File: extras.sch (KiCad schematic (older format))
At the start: 36 parts, among them P1 CONN_01X03, P2 CONN_01X03, P3 CONN_01X02, P4 CONN_01X02, P5 CONN_01X02, P6 CONN_01X02, U1 LT3472, U2 LMR62014, U3 LM3674

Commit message: Latest work
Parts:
- added C?: 2.2uF, symbol C
- added C?: 47pF, symbol C_Small
- added C?: 22uF, symbol C
- added C? (x2): 0.1uF, symbol C_Small
- added C?: 4.7uF, symbol C
- added L? (x2): 15uH, symbol L_Small
- added L?: 10uH, symbol L_Small
- added R?: 324k, symbol R_Small
- added R?: 549k, symbol R_Small
- added U?: LT3487, symbol LT3487
- R5: value 117k -> 118k
- U1: symbol LT3472-RESCUE-PowerRail -> LT3472
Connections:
- net labels added: -8.1V/90mA, 14.95V/45mA, CAP, FBN, FBP, RUN/SS, VIN_3V_12V
- wire segments 82 -> 161
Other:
- note added: "VNEG = -RN * 0.025 [mA] \n(40 kOhm : 1 V)"
- note added: "VPOS = 1.23 + RN * 0.025 [mA] \n(40 kOhm : 1 V)"
- moved on the sheet: P3, P4, P5, P6

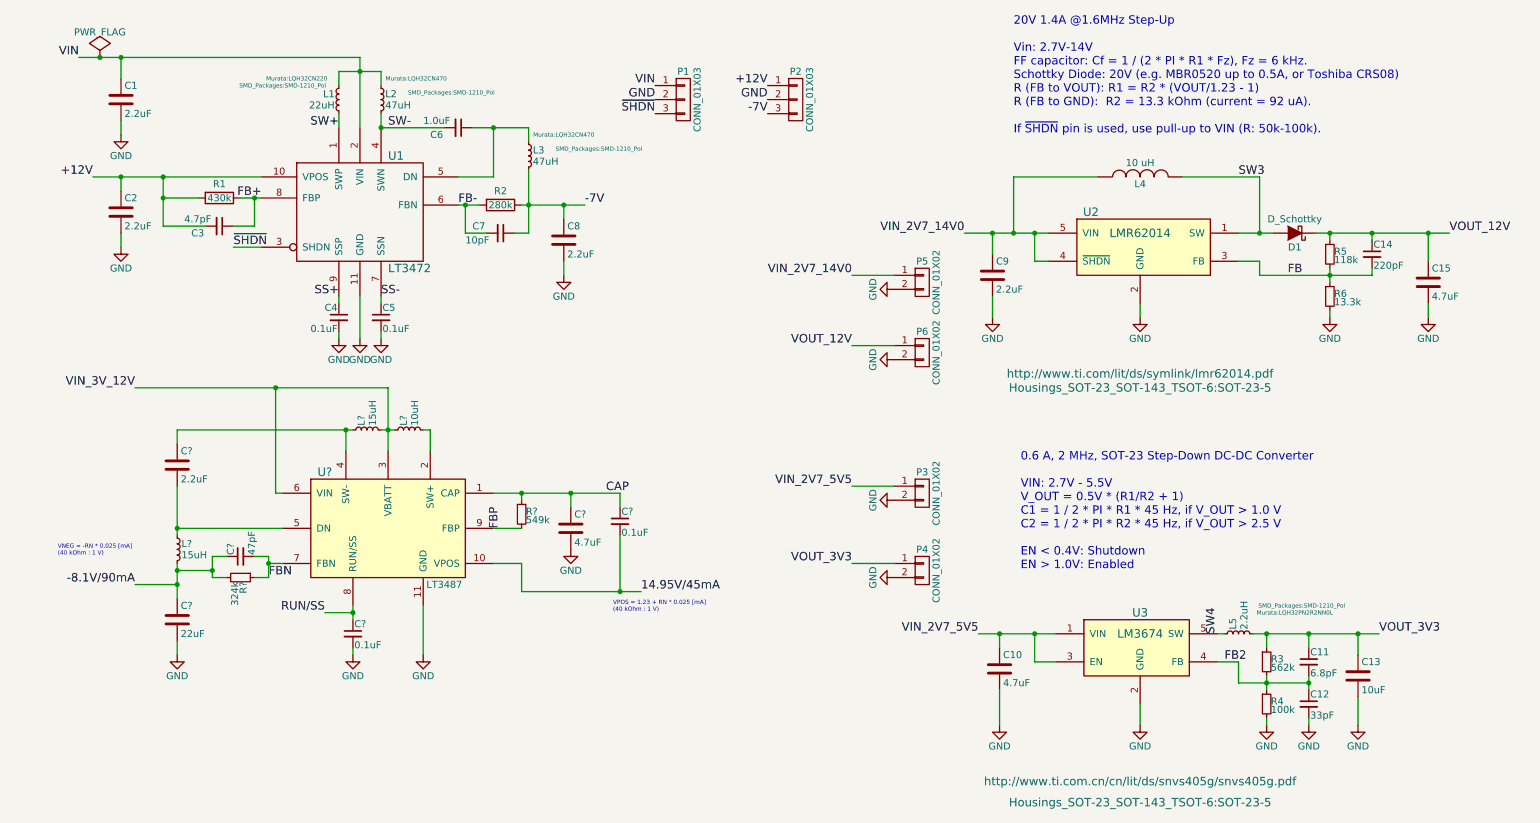
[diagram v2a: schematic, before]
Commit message: Follow ADISimPower recommendations
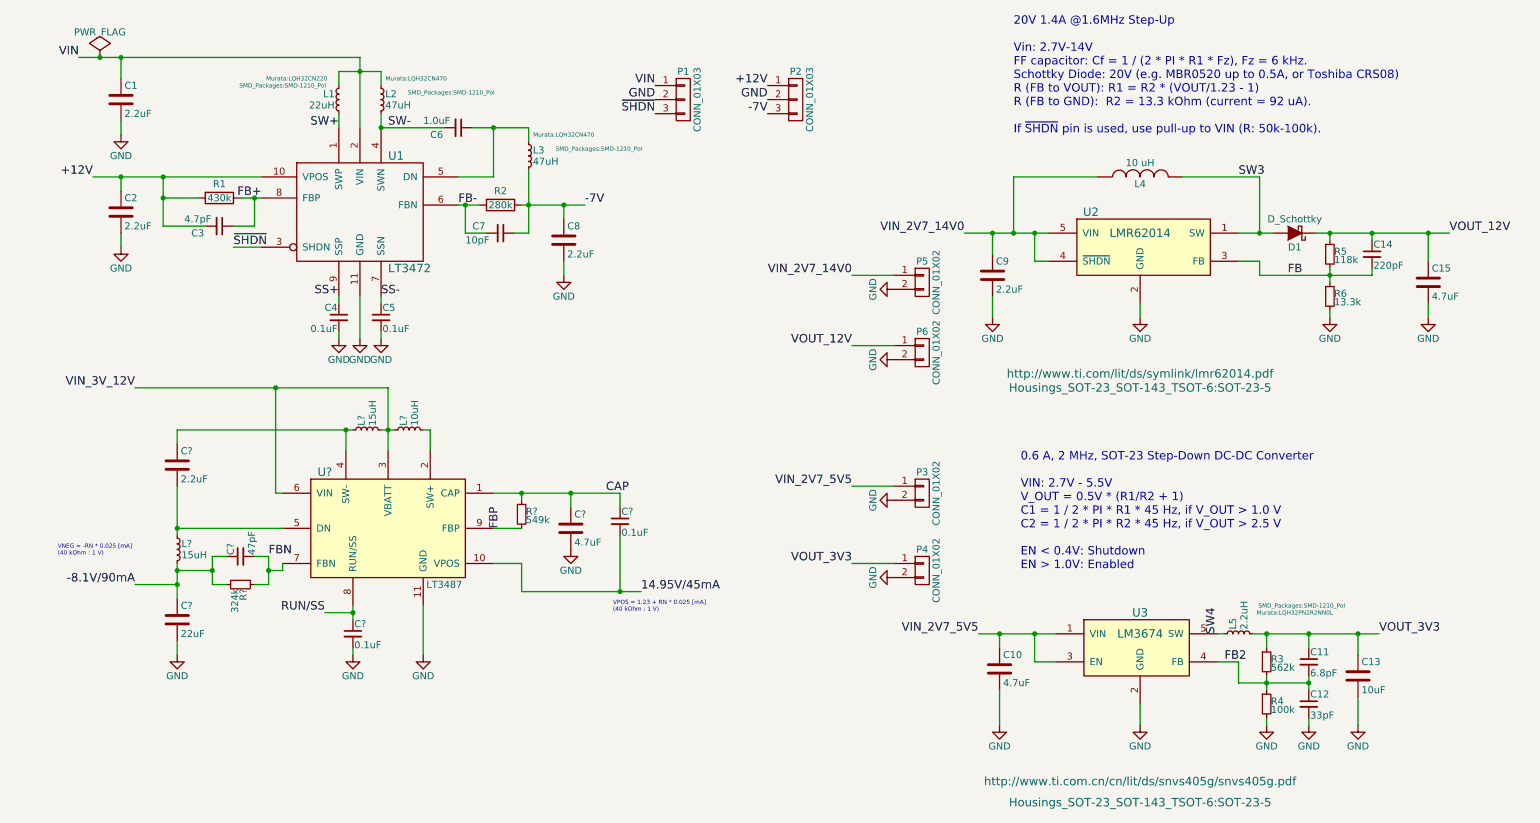
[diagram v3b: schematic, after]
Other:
- moved on the sheet: R?
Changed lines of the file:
@@
 $EndDescr
 Wire Wire Line
-	1050 950  1200 950
-Wire Wire Line
-	1200 950  1350 950
-Wire Wire Line
-	1350 950  3050 950
+	1050 950  3050 950
 $Comp
 L C C1
@@
 	2900 1150 2900 1050
 Wire Wire Line
-	2900 1050 3050 1050
-Wire Wire Line
-	3050 1050 3200 1050
+	2900 1050 3200 1050
 Connection ~ 3050 1050
 Wire Wire Line
@@
 $EndComp
 Wire Wire Line
-	1150 1800 1350 1800
-Wire Wire Line
-	1350 1800 1650 1800
-Wire Wire Line
-	1650 1800 2350 1800
-Wire Wire Line
-	2200 1950 2300 1950
-Wire Wire Line
-	2300 1950 2350 1950
+	1150 1800 2350 1800
+Wire Wire Line
+	2200 1950 2350 1950
 Wire Wire Line
 	1900 1950 1650 1950
 Wire Wire Line
-	1650 1800 1650 1950
-Wire Wire Line
-	1650 1950 1650 2150
+	1650 1800 1650 2150
 Connection ~ 1650 1800
 Wire Wire Line
@@
 $EndComp
 Wire Wire Line
-	3850 1450 4000 1450
-Wire Wire Line
-	4000 1450 4250 1450
-Wire Wire Line
-	4200 2000 4250 2000
-Wire Wire Line
-	4250 2000 4500 2000
-Wire Wire Line
-	4500 2000 4650 2000
-Wire Wire Line
-	4250 1750 4250 2000
-Wire Wire Line
-	4250 2000 4250 2200
-Wire Wire Line
-	3750 2000 3800 2000
-Wire Wire Line
-	3800 2000 3900 2000
+	3850 1450 4250 1450
+Wire Wire Line
+	4200 2000 4650 2000
+Wire Wire Line
+	4250 1750 4250 2200
+Wire Wire Line
+	3750 2000 3900 2000
 $Comp
 L C_Small C7
@@
 VIN_2V7_5V5
 Wire Wire Line
-	7450 5050 7600 5050
-Wire Wire Line
-	7600 5050 7850 5050
-Wire Wire Line
-	7850 5050 8000 5050
+	7450 5050 8000 5050
 $Comp
 L C C10
@@
 	9150 5050 9200 5050
 Wire Wire Line
-	9400 5050 9500 5050
-Wire Wire Line
-	9500 5050 9800 5050
-Wire Wire Line
-	9800 5050 10150 5050
-Wire Wire Line
-	10150 5050 10300 5050
+	9400 5050 10300 5050
 $Comp
 L R_Small R3
@@
 Connection ~ 9500 5050
 Wire Wire Line
-	9500 5350 9500 5400
-Wire Wire Line
-	9500 5400 9500 5450
-Wire Wire Line
-	9300 5400 9500 5400
-Wire Wire Line
-	9500 5400 9800 5400
-Wire Wire Line
-	9800 5350 9800 5400
-Wire Wire Line
-	9800 5400 9800 5450
+	9500 5350 9500 5450
+Wire Wire Line
+	9300 5400 9800 5400
+Wire Wire Line
+	9800 5350 9800 5450
 Connection ~ 9500 5400
 Connection ~ 9800 5400
@@
 20V 1.4A @1.6MHz Step-Up\n\nVin: 2.7V-14V\nFF capacitor: Cf = 1 / (2 * PI * R1 * Fz), Fz = 6 kHz.\nSchottky Diode: 20V (e.g. MBR0520 up to 0.5A, or Toshiba CRS08)\nR (FB to VOUT): R1 = R2 * (VOUT/1.23 - 1)\nR (FB to GND):  R2 = 13.3 kOhm (current = 92 uA).\n\nIf ~SHDN~ pin is used, use pull-up to VIN (R: 50k-100k).
 Wire Wire Line
-	7350 2200 7550 2200
-Wire Wire Line
-	7550 2200 7700 2200
-Wire Wire Line
-	7700 2200 7850 2200
-Wire Wire Line
-	7850 2200 7950 2200
+	7350 2200 7950 2200
 Connection ~ 7850 2200
 Wire Wire Line
@@
 	9450 1800 9450 2200
 Wire Wire Line
-	9300 2200 9450 2200
-Wire Wire Line
-	9450 2200 9550 2200
+	9300 2200 9550 2200
 $Comp
 L D_Schottky D1
@@
 Connection ~ 9450 2200
 Wire Wire Line
-	9850 2200 9950 2200
-Wire Wire Line
-	9950 2200 10250 2200
-Wire Wire Line
-	10250 2200 10650 2200
-Wire Wire Line
-	10650 2200 10800 2200
+	9850 2200 10800 2200
 $Comp
 L R_Small R5
@@
 Connection ~ 10250 2200
 Wire Wire Line
-	9950 2450 9950 2500
-Wire Wire Line
-	9950 2500 9950 2550
-Wire Wire Line
-	9450 2500 9950 2500
-Wire Wire Line
-	9950 2500 10250 2500
+	9950 2450 9950 2550
+Wire Wire Line
+	9450 2500 10250 2500
 Wire Wire Line
 	10250 2500 10250 2450
@@
 SW3
 Wire Wire Line
-	3050 950  3050 1050
-Wire Wire Line
-	3050 1050 3050 1450
+	3050 950  3050 1450
 $Comp
 L LT3487 U?
@@
 	2950 3750 2950 3600
 Wire Wire Line
-	1750 3600 2950 3600
-Wire Wire Line
-	2950 3600 3000 3600
-Wire Wire Line
-	3200 3600 3250 3600
-Wire Wire Line
-	3250 3600 3300 3600
-Wire Wire Line
-	3250 3300 3250 3600
-Wire Wire Line
-	3250 3600 3250 3750
+	1750 3600 3000 3600
+Wire Wire Line
+	3200 3600 3300 3600
+Wire Wire Line
+	3250 3300 3250 3750
 Connection ~ 3250 3600
 Wire Wire Line
-	1450 3300 2450 3300
-Wire Wire Line
-	2450 3300 3250 3300
+	1450 3300 3250 3300
 Wire Wire Line
 	3500 3600 3550 3600
@@
 $EndComp
 Wire Wire Line
-	1750 4000 1750 4300
-Wire Wire Line
-	1750 4300 1750 4350
+	1750 4000 1750 4350
 $Comp
 L C_Small C?
@@
 L R_Small R?
 U 1 1 56573C0F
-P 2200 4650
-F 0 "R?" H 2230 4670 50  0000 L CNN
-F 1 "324k" H 2230 4610 50  0000 L CNN
-F 2 "" H 2200 4650 60  0000 C CNN
-F 3 "" H 2200 4650 60  0000 C CNN
-	1    2200 4650
+P 2200 4700
+F 0 "R?" H 2230 4720 50  0000 L CNN
+F 1 "324k" H 2230 4660 50  0000 L CNN
+F 2 "" H 2200 4700 60  0000 C CNN
+F 3 "" H 2200 4700 60  0000 C CNN
+	1    2200 4700
 	0    1    1    0
 $EndComp
@@
 	2300 4500 2400 4500
 Wire Wire Line
-	2400 4500 2400 4550
-Wire Wire Line
-	2400 4550 2400 4650
-Wire Wire Line
-	2400 4550 2500 4550
-Wire Wire Line
-	2400 4650 2300 4650
-Connection ~ 2400 4550
+	2400 4500 2400 4700
+Wire Wire Line
+	2400 4600 2500 4600
+Wire Wire Line
+	2400 4700 2300 4700
+Connection ~ 2400 4600
 Wire Wire Line
 	2100 4500 2000 4500
 Wire Wire Line
-	2000 4500 2000 4600
-Wire Wire Line
-	2000 4600 2000 4650
-Wire Wire Line
-	2000 4650 2100 4650
+	2000 4500 2000 4700
+Wire Wire Line
+	2000 4700 2100 4700
 Wire Wire Line
 	2000 4600 1750 4600
 Wire Wire Line
-	1750 4550 1750 4600
-Wire Wire Line
-	1750 4600 1750 4700
-Wire Wire Line
-	1750 4700 1750 4800
+	1750 4550 1750 4800
 Connection ~ 2000 4600
 Wire Wire Line
@@
 $EndComp
 Wire Wire Line
-	3000 4850 3000 4900
-Wire Wire Line
-	3000 4900 3000 4950
+	3000 4850 3000 4950
 $Comp
 L GND #PWR?
@@
 	4000 4300 4200 4300
 Wire Wire Line
-	4000 4050 4200 4050
-Wire Wire Line
-	4200 4050 4550 4050
-Wire Wire Line
-	4550 4050 4900 4050
+	4000 4050 4900 4050
 Wire Wire Line
 	4200 4050 4200 4100
@@
 	4200 4550 4200 4750
 Wire Wire Line
-	4200 4750 4900 4750
-Wire Wire Line
-	4900 4750 5050 4750
+	4200 4750 5050 4750
 Wire Wire Line
 	4900 4750 4900 4350
@@
 Text Label 1450 3300 2    60   ~ 0
 VIN_3V_12V
-Text Label 2400 4650 0    60   ~ 0
+Text Label 2400 4500 0    60   ~ 0
 FBN
 Text Label 4050 4300 1    60   ~ 0
@@
 Text Notes 4850 4900 0    30   ~ 0
 VPOS = 1.23 + RN * 0.025 [mA] \n(40 kOhm : 1 V)
+Wire Wire Line
+	2500 4600 2500 4550
 $EndSCHEMATC

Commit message: Some change
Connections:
- net -8.1V/90mA: no longer R?.2
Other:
- moved on the sheet: R?
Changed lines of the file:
@@
 	2900 1150 2900 1050
 Wire Wire Line
-	2900 1050 3200 1050
+	2900 1050 3050 1050
+Wire Wire Line
+	3050 1050 3200 1050
 Connection ~ 3050 1050
 Wire Wire Line
@@
 $EndComp
 Wire Wire Line
-	1150 1800 2350 1800
-Wire Wire Line
-	2200 1950 2350 1950
+	1150 1800 1350 1800
+Wire Wire Line
+	1350 1800 1650 1800
+Wire Wire Line
+	1650 1800 2350 1800
+Wire Wire Line
+	2200 1950 2300 1950
+Wire Wire Line
+	2300 1950 2350 1950
 Wire Wire Line
 	1900 1950 1650 1950
 Wire Wire Line
-	1650 1800 1650 2150
+	1650 1800 1650 1950
+Wire Wire Line
+	1650 1950 1650 2150
 Connection ~ 1650 1800
 Wire Wire Line
@@
 $EndComp
 Wire Wire Line
-	3850 1450 4250 1450
-Wire Wire Line
-	4200 2000 4650 2000
-Wire Wire Line
-	4250 1750 4250 2200
-Wire Wire Line
-	3750 2000 3900 2000
+	3850 1450 4000 1450
+Wire Wire Line
+	4000 1450 4250 1450
+Wire Wire Line
+	4200 2000 4250 2000
+Wire Wire Line
+	4250 2000 4500 2000
+Wire Wire Line
+	4500 2000 4650 2000
+Wire Wire Line
+	4250 1750 4250 2000
+Wire Wire Line
+	4250 2000 4250 2200
+Wire Wire Line
+	3750 2000 3800 2000
+Wire Wire Line
+	3800 2000 3900 2000
 $Comp
 L C_Small C7
@@
 VIN_2V7_5V5
 Wire Wire Line
-	7450 5050 8000 5050
+	7450 5050 7600 5050
+Wire Wire Line
+	7600 5050 7850 5050
+Wire Wire Line
+	7850 5050 8000 5050
 $Comp
 L C C10
@@
 	9150 5050 9200 5050
 Wire Wire Line
-	9400 5050 10300 5050
+	9400 5050 9500 5050
+Wire Wire Line
+	9500 5050 9800 5050
+Wire Wire Line
+	9800 5050 10150 5050
+Wire Wire Line
+	10150 5050 10300 5050
 $Comp
 L R_Small R3
@@
 Connection ~ 9500 5050
 Wire Wire Line
-	9500 5350 9500 5450
-Wire Wire Line
-	9300 5400 9800 5400
-Wire Wire Line
-	9800 5350 9800 5450
+	9500 5350 9500 5400
+Wire Wire Line
+	9500 5400 9500 5450
+Wire Wire Line
+	9300 5400 9500 5400
+Wire Wire Line
+	9500 5400 9800 5400
+Wire Wire Line
+	9800 5350 9800 5400
+Wire Wire Line
+	9800 5400 9800 5450
 Connection ~ 9500 5400
 Connection ~ 9800 5400
@@
 20V 1.4A @1.6MHz Step-Up\n\nVin: 2.7V-14V\nFF capacitor: Cf = 1 / (2 * PI * R1 * Fz), Fz = 6 kHz.\nSchottky Diode: 20V (e.g. MBR0520 up to 0.5A, or Toshiba CRS08)\nR (FB to VOUT): R1 = R2 * (VOUT/1.23 - 1)\nR (FB to GND):  R2 = 13.3 kOhm (current = 92 uA).\n\nIf ~SHDN~ pin is used, use pull-up to VIN (R: 50k-100k).
 Wire Wire Line
-	7350 2200 7950 2200
+	7350 2200 7550 2200
+Wire Wire Line
+	7550 2200 7700 2200
+Wire Wire Line
+	7700 2200 7850 2200
+Wire Wire Line
+	7850 2200 7950 2200
 Connection ~ 7850 2200
 Wire Wire Line
@@
 	9450 1800 9450 2200
 Wire Wire Line
-	9300 2200 9550 2200
+	9300 2200 9450 2200
+Wire Wire Line
+	9450 2200 9550 2200
 $Comp
 L D_Schottky D1
@@
 Connection ~ 9450 2200
 Wire Wire Line
-	9850 2200 10800 2200
+	9850 2200 9950 2200
+Wire Wire Line
+	9950 2200 10250 2200
+Wire Wire Line
+	10250 2200 10650 2200
+Wire Wire Line
+	10650 2200 10800 2200
 $Comp
 L R_Small R5
@@
 Connection ~ 10250 2200
 Wire Wire Line
-	9950 2450 9950 2550
-Wire Wire Line
-	9450 2500 10250 2500
+	9950 2450 9950 2500
+Wire Wire Line
+	9950 2500 9950 2550
+Wire Wire Line
+	9450 2500 9950 2500
+Wire Wire Line
+	9950 2500 10250 2500
 Wire Wire Line
 	10250 2500 10250 2450
@@
 SW3
 Wire Wire Line
-	3050 950  3050 1450
+	3050 950  3050 1050
+Wire Wire Line
+	3050 1050 3050 1450
 $Comp
 L LT3487 U?
@@
 	2950 3750 2950 3600
 Wire Wire Line
-	1750 3600 3000 3600
-Wire Wire Line
-	3200 3600 3300 3600
-Wire Wire Line
-	3250 3300 3250 3750
+	1750 3600 2950 3600
+Wire Wire Line
+	2950 3600 3000 3600
+Wire Wire Line
+	3200 3600 3250 3600
+Wire Wire Line
+	3250 3600 3300 3600
+Wire Wire Line
+	3250 3300 3250 3600
+Wire Wire Line
+	3250 3600 3250 3750
 Connection ~ 3250 3600
 Wire Wire Line
-	1450 3300 3250 3300
+	1450 3300 2450 3300
+Wire Wire Line
+	2450 3300 3250 3300
 Wire Wire Line
 	3500 3600 3550 3600
@@
 $EndComp
 Wire Wire Line
-	1750 4000 1750 4350
+	1750 4000 1750 4300
+Wire Wire Line
+	1750 4300 1750 4350
 $Comp
 L C_Small C?
@@
 L R_Small R?
 U 1 1 56573C0F
-P 2200 4700
-F 0 "R?" H 2230 4720 50  0000 L CNN
-F 1 "324k" H 2230 4660 50  0000 L CNN
-F 2 "" H 2200 4700 60  0000 C CNN
-F 3 "" H 2200 4700 60  0000 C CNN
-	1    2200 4700
+P 2200 4650
+F 0 "R?" H 2230 4670 50  0000 L CNN
+F 1 "324k" H 2230 4610 50  0000 L CNN
+F 2 "" H 2200 4650 60  0000 C CNN
+F 3 "" H 2200 4650 60  0000 C CNN
+	1    2200 4650
 	0    1    1    0
 $EndComp
@@
 	2400 4600 2500 4600
 Wire Wire Line
-	2400 4700 2300 4700
-Connection ~ 2400 4600
+	2400 4550 2500 4550
+Wire Wire Line
+	2400 4650 2300 4650
+Connection ~ 2400 4550
 Wire Wire Line
 	2100 4500 2000 4500
@@
 	2000 4600 1750 4600
 Wire Wire Line
-	1750 4550 1750 4800
+	1750 4550 1750 4600
+Wire Wire Line
+	1750 4600 1750 4700
+Wire Wire Line
+	1750 4700 1750 4800
 Connection ~ 2000 4600
 Wire Wire Line
@@
 $EndComp
 Wire Wire Line
-	3000 4850 3000 4950
+	3000 4850 3000 4900
+Wire Wire Line
+	3000 4900 3000 4950
 $Comp
 L GND #PWR?
@@
 	4000 4300 4200 4300
 Wire Wire Line
-	4000 4050 4900 4050
+	4000 4050 4200 4050
+Wire Wire Line
+	4200 4050 4550 4050
+Wire Wire Line
+	4550 4050 4900 4050
 Wire Wire Line
 	4200 4050 4200 4100
@@
 	4200 4550 4200 4750
 Wire Wire Line
-	4200 4750 5050 4750
+	4200 4750 4900 4750
+Wire Wire Line
+	4900 4750 5050 4750
 Wire Wire Line
 	4900 4750 4900 4350
@@
 Text Label 1450 3300 2    60   ~ 0
 VIN_3V_12V
-Text Label 2400 4500 0    60   ~ 0
+Text Label 2400 4650 0    60   ~ 0
 FBN
 Text Label 4050 4300 1    60   ~ 0
@@
 Text Notes 4850 4900 0    30   ~ 0
 VPOS = 1.23 + RN * 0.025 [mA] \n(40 kOhm : 1 V)
-Wire Wire Line
-	2500 4600 2500 4550
 $EndSCHEMATC

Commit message: More work
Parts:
- C1, C14, C15, C2, C3, C4, C5, C6, C7, C8, C9: footprint Capacitors_SMD:C_0603 -> smd:SM0603
- C50, C54: renamed from C?; footprint (none) -> smd:SM0805
- C51: renamed from C?; footprint (none) -> smd:SM1206
- C52, C53, C55: renamed from C?; footprint (none) -> smd:SM0603
- L1, L2, L3: footprint SMD_Packages:SMD-1210_Pol -> engstad:diode-smd-1210-lqh32c
- L18, L19, L20: renamed from L?; footprint (none) -> engstad:diode-smd-1210-lqh32c
- L5: footprint SMD_Packages:SMD-1210_Pol -> engstad:diode-smd-1210
- P1, P2: footprint Pin_Headers:Pin_Header_Straight_1x03 -> xess:HDR_1x3
- P3, P4, P5, P6: footprint Pin_Headers:Pin_Header_Straight_1x02 -> xess:HDR_1x2
- R1, R2, R5, R6: footprint Resistors_SMD:R_0603 -> smd:SM0603
- R22, R23: renamed from R?; footprint (none) -> smd:SM0603
- U1: footprint Housings_DFN_QFN:DFN-10-1EP_3x3mm_Pitch0.5mm -> w_smd_qfn:dfn10-3x3
- U2, U3: footprint Housings_SOT-23_SOT-143_TSOT-6:SOT-23-5 -> w_smd_trans:sot23-5
- gave numbers to parts that had none: 1
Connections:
- net -8.1V/90mA: now also R22.2
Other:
- moved on the sheet: R22

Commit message: Tiny fixes
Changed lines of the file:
@@
 U 1 1 5612AA18
 P 3050 2050
-F 0 "U1" H 3250 2450 60  0000 L CNN
-F 1 "LT3472" H 3250 1650 60  0000 L CNN
+F 0 "U1" H 2600 2450 60  0000 L CNN
+F 1 "LT3472" H 2900 2050 60  0000 L CNN
 F 2 "w_smd_qfn:dfn10-3x3" H 3050 2050 60  0001 C CNN
 F 3 "" H 3050 2050 60  0000 C CNN
@@
 Wire Wire Line
 	2400 4700 2300 4700
+$Comp
+L PWR_FLAG #FLG023
+U 1 1 5675E5DD
+P 7450 2150
+F 0 "#FLG023" H 7450 2245 50  0001 C CNN
+F 1 "PWR_FLAG" H 7450 2374 50  0000 C CNN
+F 2 "" H 7450 2150 50  0000 C CNN
+F 3 "" H 7450 2150 50  0000 C CNN
+	1    7450 2150
+	1    0    0    -1
+$EndComp
+$Comp
+L PWR_FLAG #FLG024
+U 1 1 5675E67F
+P 7500 5000
+F 0 "#FLG024" H 7500 5095 50  0001 C CNN
+F 1 "PWR_FLAG" H 7500 5224 50  0000 C CNN
+F 2 "" H 7500 5000 50  0000 C CNN
+F 3 "" H 7500 5000 50  0000 C CNN
+	1    7500 5000
+	1    0    0    -1
+$EndComp
+$Comp
+L PWR_FLAG #FLG025
+U 1 1 5675E9BA
+P 1600 3250
+F 0 "#FLG025" H 1600 3345 50  0001 C CNN
+F 1 "PWR_FLAG" H 1600 3474 50  0000 C CNN
+F 2 "" H 1600 3250 50  0000 C CNN
+F 3 "" H 1600 3250 50  0000 C CNN
+	1    1600 3250
+	1    0    0    -1
+$EndComp
+Wire Wire Line
+	7450 2150 7450 2200
+Connection ~ 7450 2200
+Wire Wire Line
+	7500 5000 7500 5050
+Connection ~ 7500 5050
+Wire Wire Line
+	1600 3250 1600 3300
+Connection ~ 1600 3300
 $EndSCHEMATC

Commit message: Safety checkin.
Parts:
- C1, C10, C13, C15, C2, C50, C51, C54, C8, C9: symbol C -> Device:C
- C11, C12, C14, C3, C4, C5, C52, C53, C55, C6, C7: symbol C_Small -> Device:C_Small
- D1: symbol D_Schottky -> Device:D_Schottky
- L1, L18, L19, L2, L20, L3, L5: symbol L_Small -> Device:L_Small
- L4: symbol INDUCTOR -> Device:L
- P1, P2: symbol CONN_01X03 -> Connector_Generic:Conn_01x03
- P3, P4, P5, P6: symbol CONN_01X02 -> Connector_Generic:Conn_01x02
- R1, R2: symbol R -> Device:R
- R22, R23, R3, R4, R5, R6: symbol R_Small -> Device:R_Small
- U1: symbol LT3472 -> Engstad:LT3472
- U2: symbol LMR62014 -> Engstad:LMR62014
- U3: symbol LM3674 -> Engstad:LM3674
- U7: symbol LT3487 -> Engstad:LT3487
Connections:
- net SW-: no longer C6.2, L2.2, U1.4 (SWN)
- new net: C6.2, L2.2, U1.4 (SWN)
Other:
- moved on the sheet: C2, C3, C4, C5, C6, C7, C8, L1, L2, L3, R1, R2
